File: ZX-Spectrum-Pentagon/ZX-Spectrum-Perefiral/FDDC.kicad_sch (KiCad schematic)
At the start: 71 parts

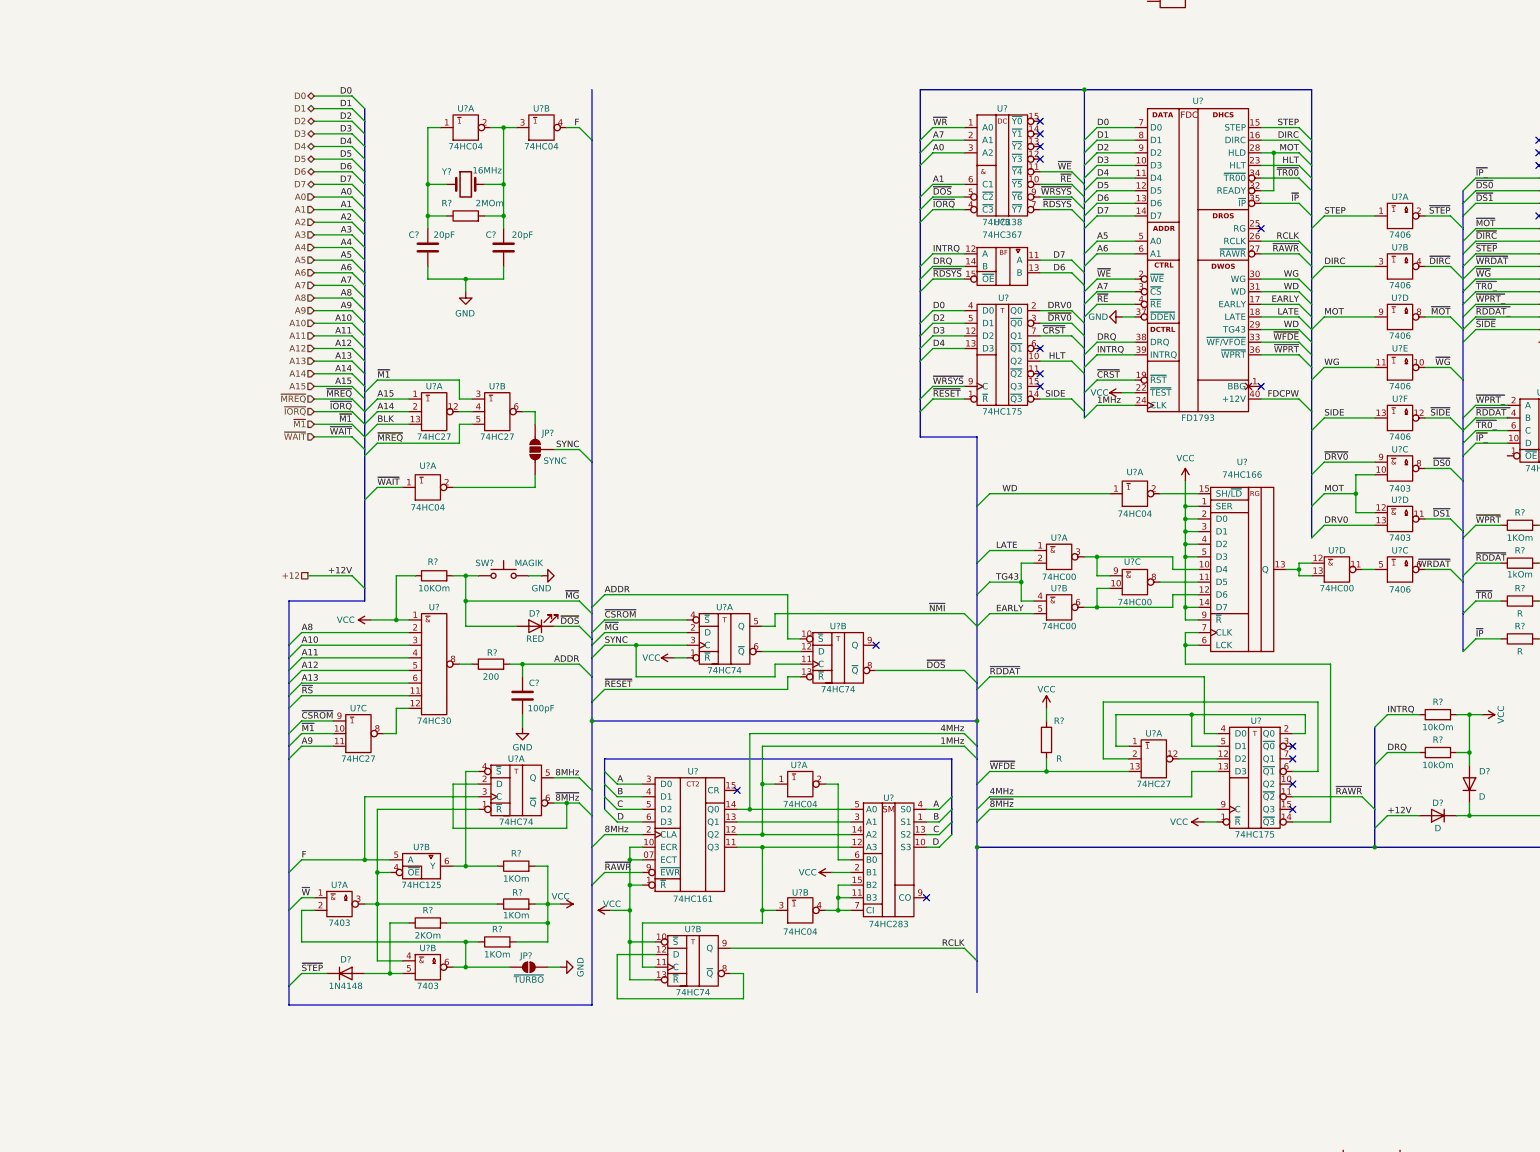
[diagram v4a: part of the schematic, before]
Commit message: improve schematic fdc
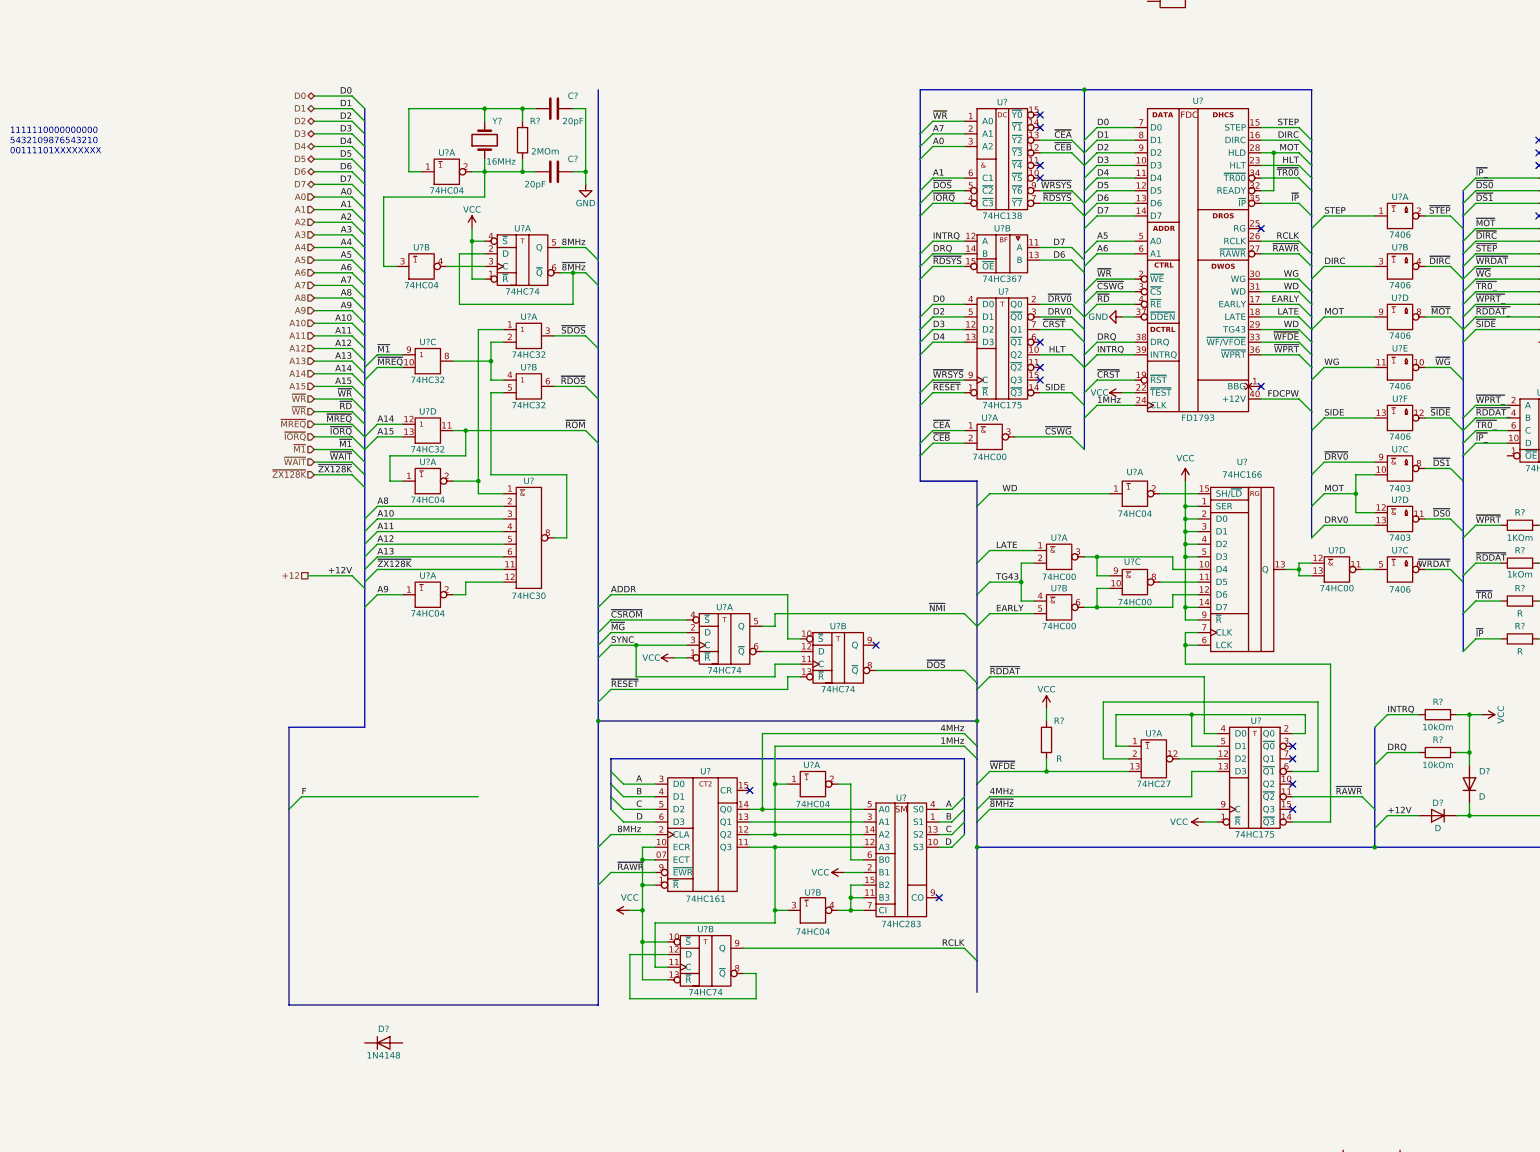
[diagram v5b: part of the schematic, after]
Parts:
- removed C?: 100pF, Capacitor_SMD:C_0805_2012Metric, symbol Device:C
- removed D?: RED, LED_SMD:LED_0805_2012Metric, symbol Device:LED
- removed JP?: ~{TURBO}, symbol Jumper:SolderJumper_2_Open
- removed JP?: SYNC, Jumper:SolderJumper-3_P1.3mm_Open_RoundedPad1.0x1.5mm, symbol Jumper:SolderJumper_3_Open
- removed R? (x3): 1KOm, Resistor_SMD:R_0805_2012Metric, symbol Device:R
- removed R?: 2KOm, Resistor_SMD:R_0805_2012Metric, symbol Device:R
- removed R?: 200, Resistor_SMD:R_0805_2012Metric, symbol Device:R
- removed R?: 10KOm, Resistor_SMD:R_0805_2012Metric, symbol Device:R
- removed SW?: MAGIK, Button_Switch_THT:SW_Tactile_SPST_Angled_PTS645Vx31-2LFS, symbol Switch:SW_Push
- removed U? (x3): 74HC27, symbol 74IEC:74HC27
- removed U?: 74HC125, symbol 74IEC:74HC125
- removed U? (x2): 7403, symbol 74IEC:7403
- removed U?: 74HC04, symbol 74IEC:74HC04
- added U? (x4): 74HC32, symbol 74IEC:74HC32
- added U?: 74HC00, symbol 74IEC:74HC00
- added U? (x2): 74HC04, Package_DIP:DIP-14_W7.62mm, symbol 74IEC:74HC04
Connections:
- net A14: now also U?.12 (A)
- net A15: now also U?.13 (B)
- net A7: no longer U?.3 (~{CS})
- net A9: now also U?.1 (A)
- net DRV0: now also U?.3 (~{Q0}); no longer U?.2 (Q0)
- net F: no longer U?.3 (C), U?.4 (~{Y})
- net GND: now also U?.7 (GND), U?.7 (GND), U?.7 (GND), U?.7 (GND), U?.7 (GND), U?.7 (GND), U?.7 (GND)
- net VCC: now also U?.1 (~{R}), U?.4 (~{S}), U?.14 (VCC), U?.14 (VCC), U?.14 (VCC), U?.14 (VCC), U?.14 (VCC), U?.14 (VCC), U?.14 (VCC); no longer U?.1 (A)
- net ~{DRV0}: now also U?.2 (Q0); no longer U?.3 (~{Q0})
- net ~{DS0}: now also U?.11 (~{Y}); no longer U?.8 (~{Y})
- net ~{DS1}: now also U?.8 (~{Y}); no longer U?.11 (~{Y})
- net ~{M1}: now also U?.9 (A)
- net ~{MREQ}: now also U?.10 (B)
- net ~{STEP}: no longer D?.1 (K)
- net ~{WR}: now also U?.2 (~{WE}), U?.4 (~{RE})
- net at C?.2, R?.2, Y?.2: now also U?.1 (A); no longer U?.2 (~{Y}), U?.3 (A)
- net at C?.2, R?.1, Y?.1: now also U?.2 (~{Y}), U?.3 (A); no longer U?.1 (A)
- net ~{CEB}: now reaches U?.12 (~{Y3})
- net ~{CEB}: now also U?.2 (B)
- net ~{CEA}: now reaches U?.13 (~{Y2})
- net ~{CEA}: now also U?.1 (A)
- net at U?.8 (~{Y}): now also U?.5 (B)
- net at U?.12 (H): now also U?.2 (~{Y})
- net ~{RE}: no longer names the net of U?.10 (~{Y5})
- net ~{RE}: no longer U?.4 (~{RE})
- net ~{RS} renamed ~{ZX128K}
- net ~{WE}: no longer names the net of U?.11 (~{Y4})
- net ~{WE}: no longer U?.2 (~{WE})
- new net: U?.1 (A), U?.1 (A), U?.2 (~{Y})
- new net: U?.2 (B), U?.4 (A), U?.8 (Y)
- new net: U?.3 (C), U?.4 (~{Y})
- new net ~{CSWG}: U?.3 (~{CS}), U?.3 (~{Y})
- new net ~{RDOS}: U?.6 (Y)
- new net ~{ROM}: U?.1 (A), U?.11 (Y)
- new net ~{SDOS}: U?.3 (Y)
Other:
- note added: "1111110000000000 5432109876543210 00111101XXXXXXXX"
- moved on the sheet: C?, D?, R?, U?, U?A, U?B, Y?

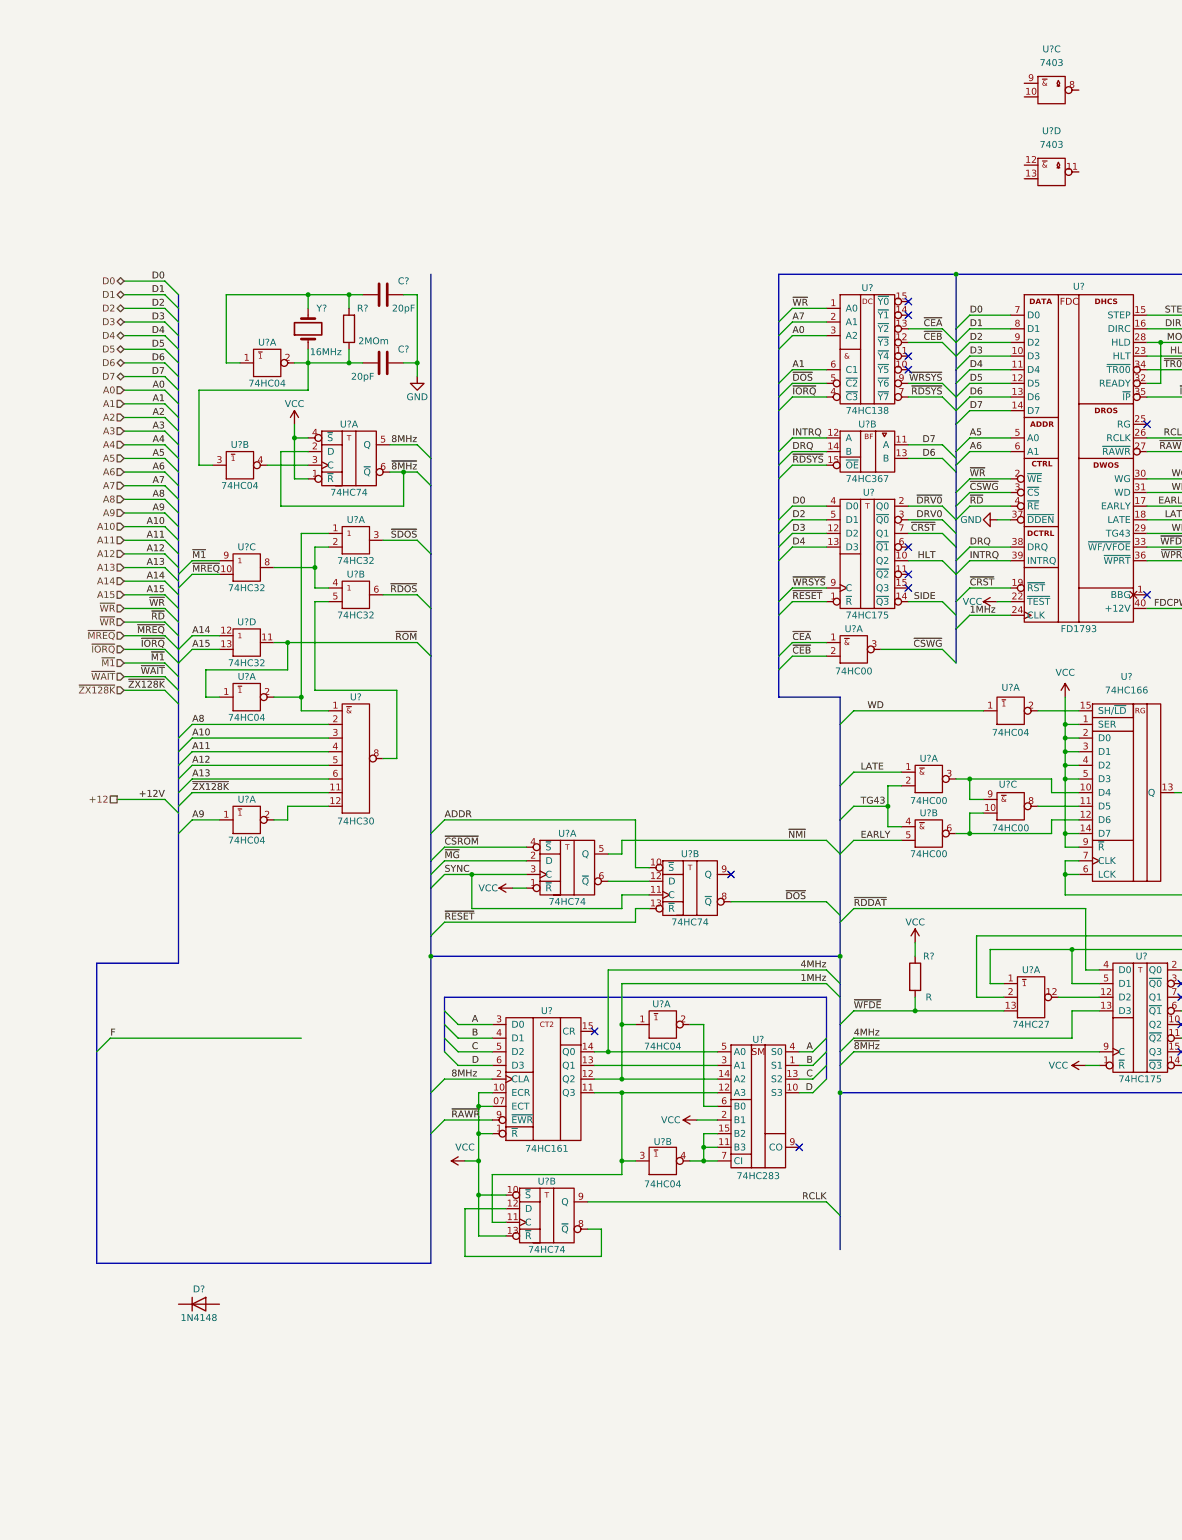
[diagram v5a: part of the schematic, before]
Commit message: fix mounting hole for ZX-Spectrum-Key-Panel improve schema fdd
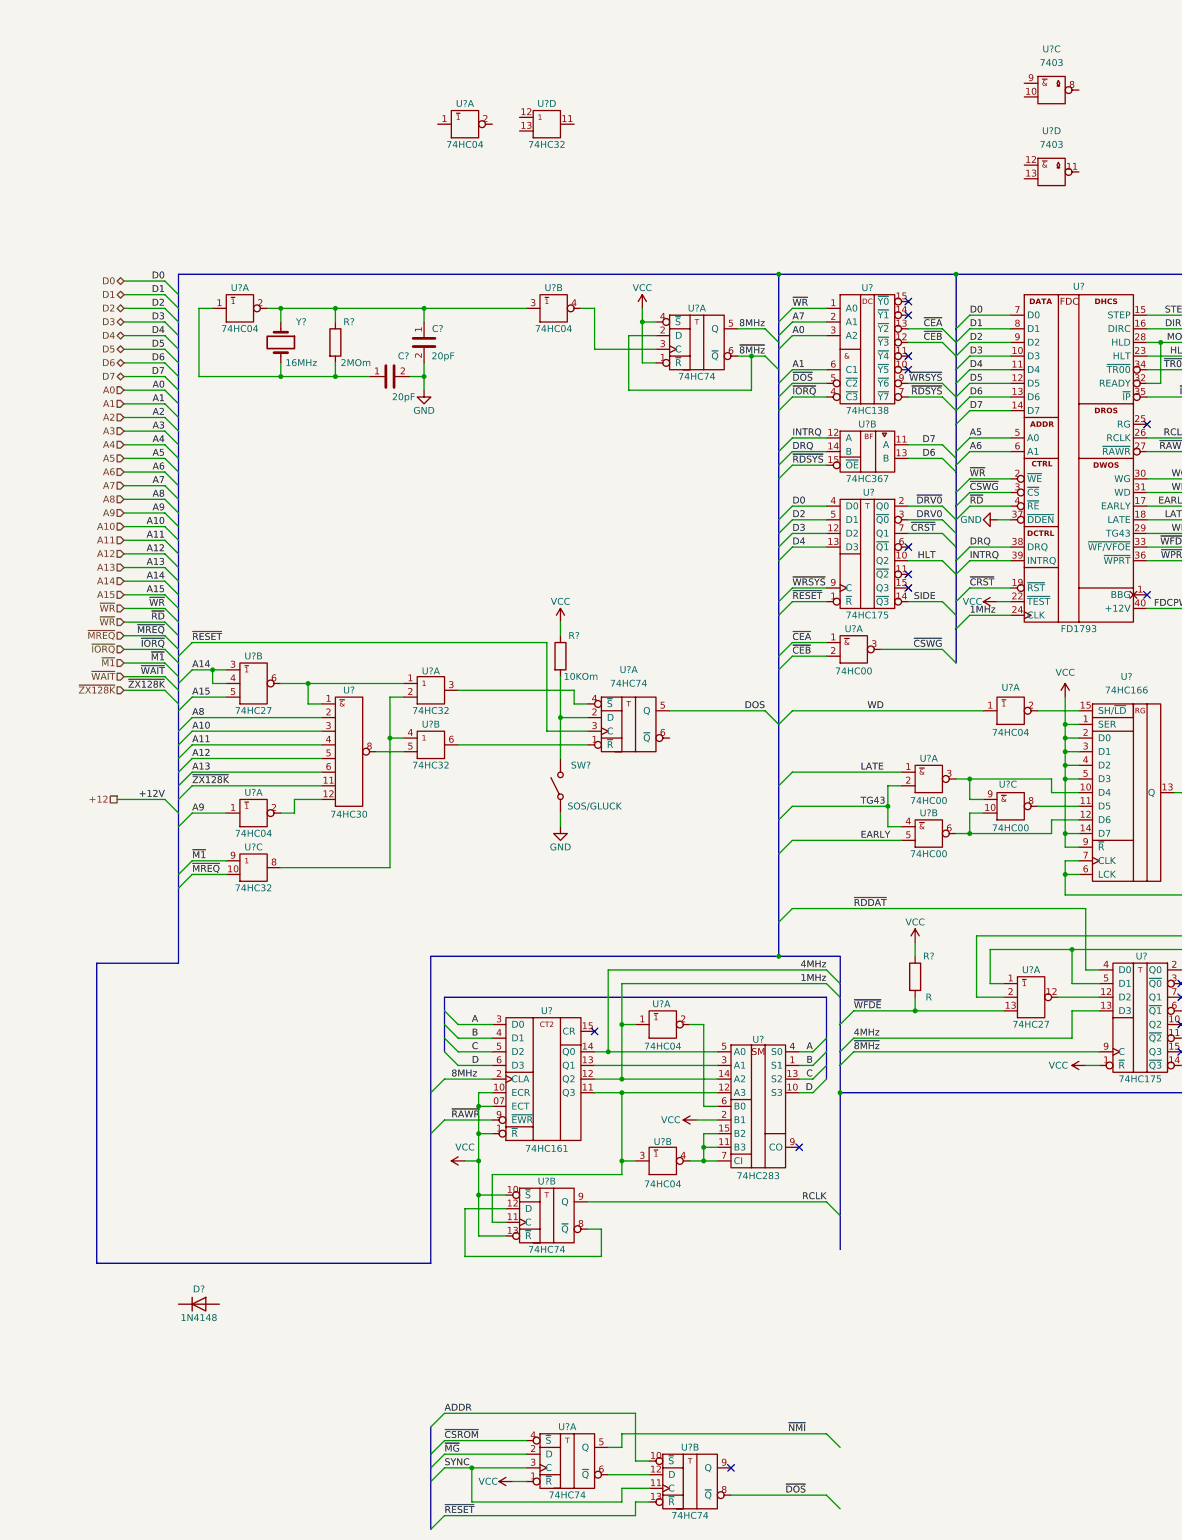
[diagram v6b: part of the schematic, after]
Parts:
- added R?: 10KOm, Resistor_SMD:R_0805_2012Metric_Pad1.20x1.40mm_HandSolder, symbol Device:R
- added SW?: SOS/GLUCK, symbol Switch:SW_SPST
- added U?: 74HC74, symbol 74IEC:74HC74
- added U?: 74HC27, symbol 74IEC:74HC27
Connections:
- net A14: now also U?.3 (A), U?.4 (B); no longer U?.12 (A)
- net A15: now also U?.5 (C); no longer U?.13 (B)
- net GND: now also C?.2, C?.2, SW?.1 (A), U?.10 (GND), U?.7 (GND); no longer C?.1, C?.1
- net VCC: now also R?.1, U?.14 (VCC), U?.14 (VCC)
- net ~{RESET}: now also U?.3 (C)
- net at U?.1 (A), U?.1 (A): now also U?.6 (~{Y}); no longer U?.2 (~{Y})
- net at R?.2, U?.1 (A), Y?.2: now also C?.1; no longer C?.2
- net at R?.1, U?.2 (~{Y}), U?.3 (A)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: now also C?.1; no longer C?.2
- net ~{RDOS}: no longer names the net of U?.6 (Y)
- net ~{RDOS}: now also U?.1 (~{R})
- net ~{ROM}: no longer names the net of U?.11 (Y)
- net ~{ROM}: no longer U?.1 (A)
- net ~{SDOS}: no longer names the net of U?.3 (Y)
- net ~{SDOS}: now also U?.4 (~{S})
- new net: R?.2, SW?.2 (B), U?.2 (D)
- new net DOS: U?.5 (Q)
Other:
- moved on the sheet: R?, U?, U?A, U?B, U?C, U?D, Y?
